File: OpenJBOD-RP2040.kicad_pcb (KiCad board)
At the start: 4 copper layers, 72.6 x 170 mm, 122 parts, among them J1 ATX-24, J2 Bus_PCI_Express_x1, J3 Conn_02x02_Counter_Clockwise, J4 UART, J6 HR911105A, J8 USB_B_Micro, J9 TEMP1, Q1 MMBT3904, Q2 MMBT3904, SW1 SW_Push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

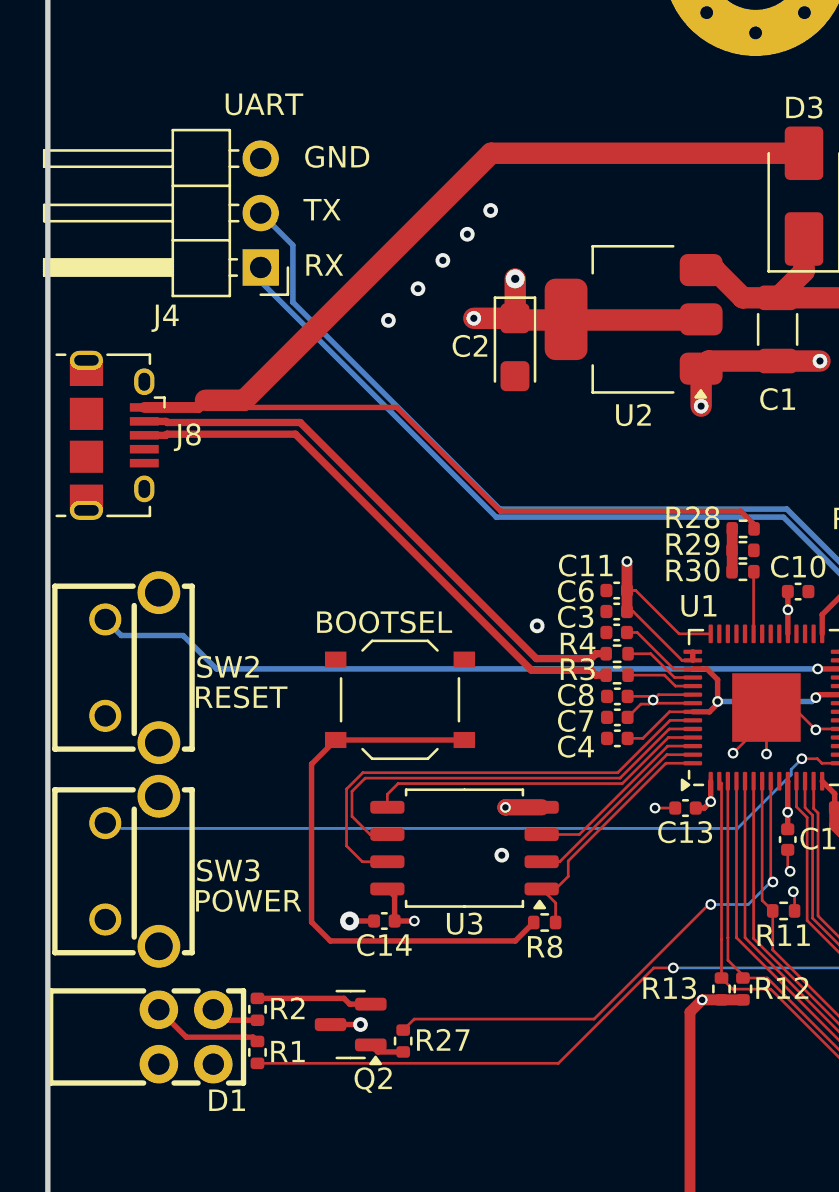
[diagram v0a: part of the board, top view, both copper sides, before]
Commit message: adjust UART header and rotate R27 for cleaner layout
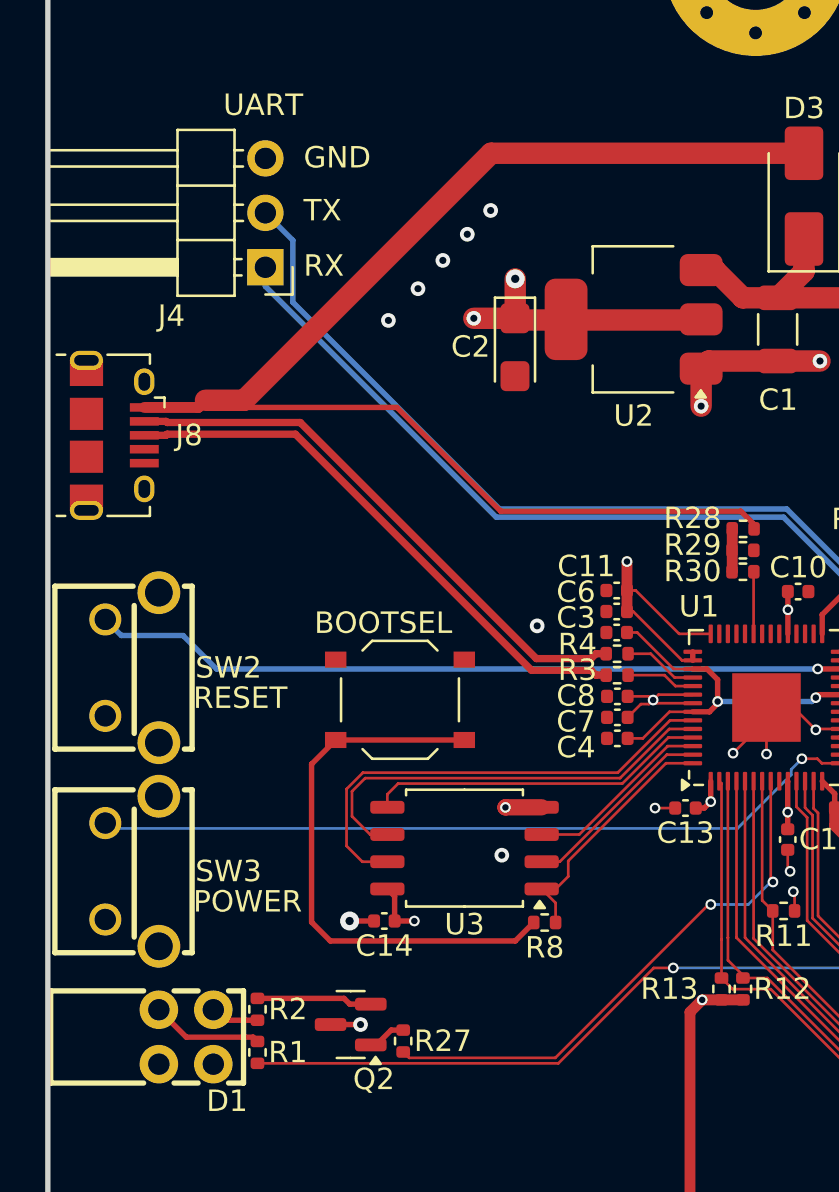
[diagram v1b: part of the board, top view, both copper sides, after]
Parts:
- moved J4 0.22 mm to (95.5, 98.6)
- turned R27 to 90 degrees
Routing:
- net /PICO_PWR: track 24.9 -> 25.5 mm

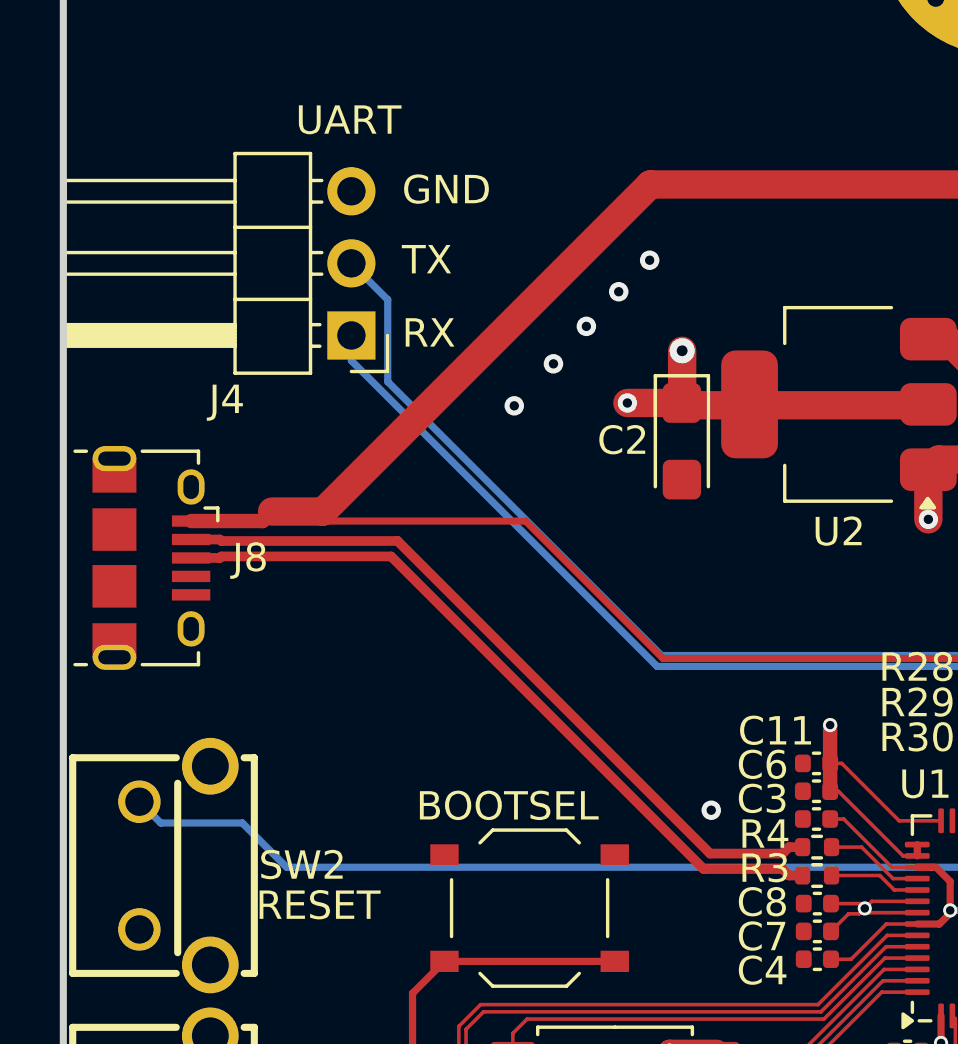
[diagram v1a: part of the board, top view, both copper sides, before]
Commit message: replace USB micro B with USB C, requires cleanup
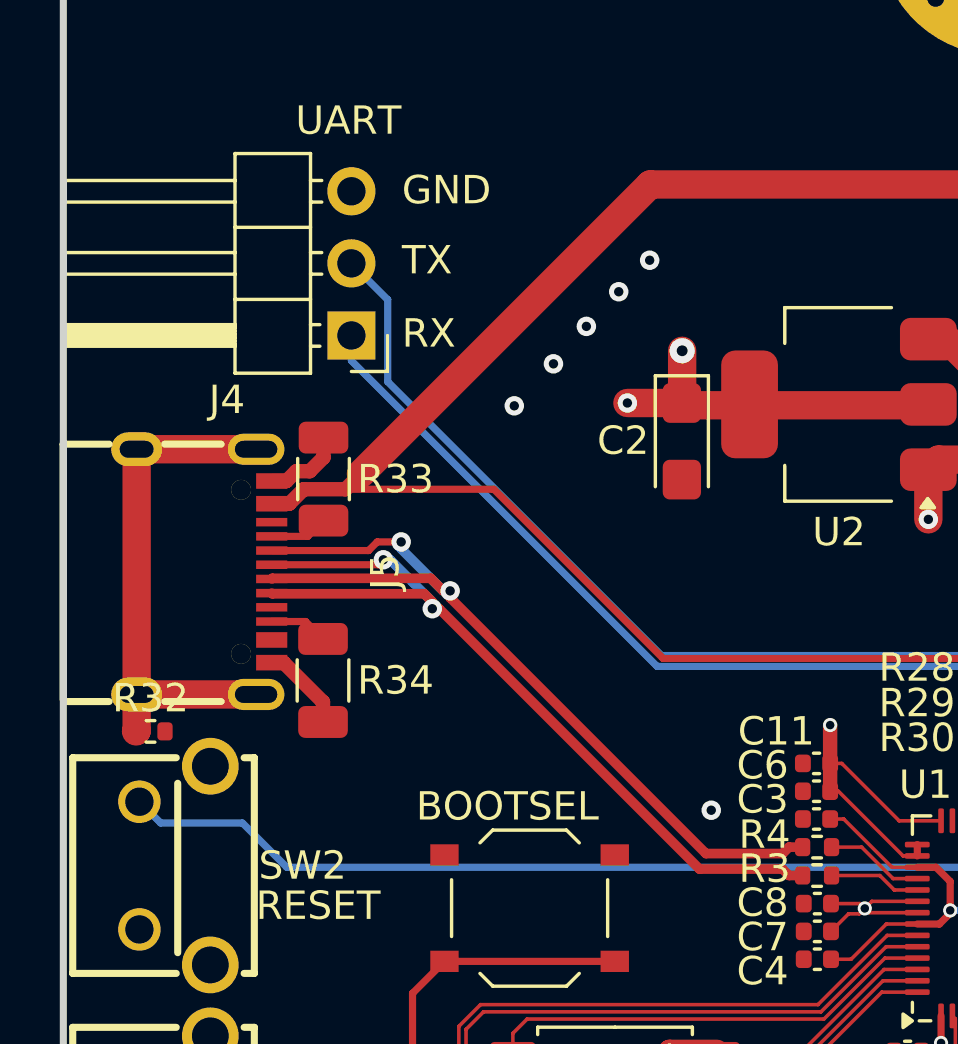
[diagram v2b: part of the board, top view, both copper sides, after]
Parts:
- removed J8: USB_B_Micro, Connector_USB:USB_Micro-B_Amphenol_10118194_Horizontal
- added J5: USB_C_Receptacle_USB2.0_16P, OpenJBOD_Library:USB-C-SMD_TYPE-C-16PIN-2MD-073, F.Cu at (90.3, 106.9)
- added R32: 1M, Resistor_SMD:R_0402_1005Metric, F.Cu at (88.4, 112.5)
- added R33: 5.11k, Resistor_SMD:R_1206_3216Metric, F.Cu at (94.5, 103.6)
- added R34: 5.11k, Resistor_SMD:R_1206_3216Metric, F.Cu at (94.5, 110.7)
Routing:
- net Net-(J5-SHIELD): track 0.00 -> 18.4 mm
- net GND: track 100.8 -> 106.8 mm
- net /USB_PWR: track 64.1 -> 58.5 mm
- net /USB_D-: track 26.2 -> 30.2 mm, vias 0 -> 2
- net /USB_D+: track 26.2 -> 29.6 mm, vias 0 -> 2
- net Net-(J5-CC2): track 0.00 -> 2.06 mm
- net Net-(J5-CC1): track 0.00 -> 2.06 mm
